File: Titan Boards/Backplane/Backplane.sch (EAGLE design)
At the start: 29 parts, among them P1 39-30-02_S, P3 39-30-04_S

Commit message: Initial schematic design backplane
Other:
- note added: "3.3V/5V Output Connector"
- note added: "Actuator Connector"
- note added: "Battery Balancer Connector"
- note added: "Coprocessor Connector"
- note added: "ESC Connector"
- note added: "Enable Signals Connector"
- note added: "I2C Control Connector"
- note added: "Kill Switch Connector"
- note added: "Lorem ipsum"
- note added: "Schematic Notes:"
- note added: "Switch Connector"
- note added: "Thurster Signal Connector"

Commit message: First final version of Titan Backplane Schematic
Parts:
- removed P1: 39-30-02_S, con-molex-mini-fit:39-30-02_S
- removed P3: 39-30-04_S, con-molex-mini-fit:39-30-04_S
- removed U$5: 929870-01-09_1, 3M_929852_Connector:929870-01-09_1
- removed U$6: 929870-01-09_2, 3M_929852_Connector:929870-01-09_2
- removed U$8: 929870-01-09_4, 3M_929852_Connector:929870-01-09_4
- added 3.3V_CONNECTOR: 39-30-04_S, con-molex-mini-fit:39-30-04_S
- added 5V_CONNECTOR: 39-30-02_S, con-molex-mini-fit:39-30-02_S
- added ACT_CONN_LED, BB_CONN_LED, COPRO_CONN_LED, ESC_CONN_LED: (no value), led:LEDCHIP-LED0603
- added I2C_CONNECTOR: 929870-01-09_4, 3M_929852_Connector:929870-01-09_4
- added KILLSWITCH_CONNECTOR: 929870-01-09_1, 3M_929852_Connector:929870-01-09_1
- added R19, R20, R21, R22: 36, rcl:R-US_R0603
- added THRUSTER_CONNECTOR: 929870-01-09_2, 3M_929852_Connector:929870-01-09_2
- renumbered U$7 to ENABLE_SIGNALS_CONNECTOR
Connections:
- removed net SPARE7: U$1.SPARE7, U$2.SPARE7, U$3.SPARE7, U$4.SPARE7, U$5.SPARE7
- new net ACT_CONN: ACT_CONN_LED.A, U$4.SPARE7
- new net BB_CONN: BB_CONN_LED.A, U$1.SPARE7
- new net COPRO_CONN: COPRO_CONN_LED.A, U$3.SPARE7
- new net ESC_CONN: ESC_CONN_LED.A, U$2.SPARE7
- new net N$12: BB_CONN_LED.C, R19.1
- new net N$13: ESC_CONN_LED.C, R20.1
- new net N$14: COPRO_CONN_LED.C, R21.1
- new net N$15: ACT_CONN_LED.C, R22.1
- net 3.3V: now also 3.3V_CONNECTOR-1.P, I2C_CONNECTOR.3.3V; no longer P3-1.P, U$8.3.3V
- net 5V: now also 5V_CONNECTOR-1.P, I2C_CONNECTOR.5V; no longer P1-1.P, U$8.5V
- net BACKPLANE_SCL: now also I2C_CONNECTOR.BACKPLANE_SCL; no longer U$8.BACKPLANE_SCL
- net BACKPLANE_SDA: now also I2C_CONNECTOR.BACKPLANE_SDA; no longer U$8.BACKPLANE_SDA
- net GND: now also 3.3V_CONNECTOR-3.P, 5V_CONNECTOR-2.P, I2C_CONNECTOR.GND, R19.2, R20.2, R21.2, R22.2; no longer P1-2.P, P3-3.P, U$8.GND
- net KILL_SWITCH: now also KILLSWITCH_CONNECTOR.KILL_SWITCH; no longer U$5.KILL_SWITCH
- net PWM_1: now also THRUSTER_CONNECTOR.PWM_1; no longer U$6.PWM_1
- net PWM_2: now also THRUSTER_CONNECTOR.PWM_2; no longer U$6.PWM_2
- net PWM_3: now also THRUSTER_CONNECTOR.PWM_3; no longer U$6.PWM_3
- net PWM_4: now also THRUSTER_CONNECTOR.PWM_4; no longer U$6.PWM_4
- net PWM_5: now also THRUSTER_CONNECTOR.PWM_5; no longer U$6.PWM_5
- net PWM_6: now also THRUSTER_CONNECTOR.PWM_6; no longer U$6.PWM_6
- net PWM_7: now also THRUSTER_CONNECTOR.PWM_7; no longer U$6.PWM_7
- net PWM_8: now also THRUSTER_CONNECTOR.PWM_8; no longer U$6.PWM_8
- net ROBOT_SCL: now also 3.3V_CONNECTOR-4.P, I2C_CONNECTOR.ROBOT_SCL; no longer P3-4.P, U$8.ROBOT_SCL
- net ROBOT_SDA: now also 3.3V_CONNECTOR-2.P, I2C_CONNECTOR.ROBOT_SDA; no longer P3-2.P, U$8.ROBOT_SDA
- net SPARE2: now also THRUSTER_CONNECTOR.SPARE2; no longer U$6.SPARE2
- net SPARE3: now also I2C_CONNECTOR.SPARE3; no longer U$8.SPARE3
- net SPARE4: now also I2C_CONNECTOR.SPARE4; no longer U$8.SPARE4
- net SPARE5: now also KILLSWITCH_CONNECTOR.SPARE5; no longer U$5.SPARE5
- net SPARE6: now also KILLSWITCH_CONNECTOR.SPARE6; no longer U$5.SPARE6
- net SWITCH_1: now also KILLSWITCH_CONNECTOR.SWITCH_1; no longer U$5.SWITCH_1
- net SWITCH_2: now also KILLSWITCH_CONNECTOR.SWITCH_2; no longer U$5.SWITCH_2
- net SWITCH_3: now also KILLSWITCH_CONNECTOR.SWITCH_3; no longer U$5.SWITCH_3
- net SWITCH_4: now also KILLSWITCH_CONNECTOR.SWITCH_4; no longer U$5.SWITCH_4
- net SWITCH_5: now also KILLSWITCH_CONNECTOR.SWITCH_5; no longer U$5.SWITCH_5
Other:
- note added: "3.3V/5V Connectors"
- note added: "Administrative Notes: Board Name: Titan Backplane Schematic Creation: 08/2020 Schematic Designer: Dylan Trainor Electrical Lead: Phillip Barker"
- note added: "Board Connected Indicators"
- note added: "Part Notes: Board Connectors: 5530843-6 56 Position Female Connector Non Specified - Dual Edge Gold 0.100 in (2.54mm) Black https://www.digikey.com/product-detail/en/te-connectivity-amp-connectors/5530843-6/A31719-ND/770545 Killswitch Connector: 929870-01-09_1 Thruster Signal Connector: 929870-01-09_2 Enable Signals Connector: 929870-01-09_3 I2C Control Connector: 929870-01-09_4 9 Position Recept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"
- note removed: "3.3V/5V Output Connector"
- note removed: "Lorem ipsum"
- moved on the sheet: R1, R10, R11, R12, R13, R14, R15, R16, R17, R18, R2, R3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

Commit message: Titan Backplane Final Version 1
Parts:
- removed 3.3V_CONNECTOR: 39-30-04_S, con-molex-mini-fit:39-30-04_S
- removed ENABLE_SIGNALS_CONNECTOR: 929870-01-09_3, 3M_929852_Connector:929870-01-09_3
- removed I2C_CONNECTOR: 929870-01-09_4, 3M_929852_Connector:929870-01-09_4
- removed KILLSWITCH_CONNECTOR: 929870-01-09_1, 3M_929852_Connector:929870-01-09_1
- removed R1, R10, R11, R12, R13, R14, R2, R3, R4, R5, R6, R7, R8, R9: 10k, rcl:R-US_R0603
- removed THRUSTER_CONNECTOR: 929870-01-09_2, 3M_929852_Connector:929870-01-09_2
- added AUX_I2C_CONNECTOR1, ROBOT_I2C_CONNECTOR: 39-30-04_S, con-molex-mini-fit:39-30-04_S
- added TESTPIN_CONNECTOR: 929870-01-09_4, 3M_929852_Connector:929870-01-09_4
- SWITCH_CONNECTOR: value 39-30-08_S -> 39-30-02_S; device con-molex-mini-fit:39-30-08_S -> con-molex-mini-fit:39-30-02_S
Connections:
- net 12V_ON/OFF: no longer ENABLE_SIGNALS_CONNECTOR.12V_ON/OFF
- net 3.3V: now also AUX_I2C_CONNECTOR1-1.P, ROBOT_I2C_CONNECTOR-1.P, TESTPIN_CONNECTOR.3.3V; no longer 3.3V_CONNECTOR-1.P, I2C_CONNECTOR.3.3V, R10.1, R11.1, R12.1, R13.1, R14.1, R9.1
- net 3.3V_ON/OFF: no longer ENABLE_SIGNALS_CONNECTOR.3.3V_ON/OFF
- net 5V: now also SWITCH_CONNECTOR-1.P, TESTPIN_CONNECTOR.5V; no longer I2C_CONNECTOR.5V, R1.1, R2.1, R3.1, R4.1, R5.1, R6.1, R7.1, R8.1
- net 5V_ON/OFF: no longer ENABLE_SIGNALS_CONNECTOR.5V_ON/OFF
- net ACOUSTIC_ON/OFF: no longer ENABLE_SIGNALS_CONNECTOR.ACOUSTIC_ON/OFF
- net BACKPLANE_SCL: now also TESTPIN_CONNECTOR.BACKPLANE_SCL; no longer I2C_CONNECTOR.BACKPLANE_SCL
- net BACKPLANE_SDA: now also TESTPIN_CONNECTOR.BACKPLANE_SDA; no longer I2C_CONNECTOR.BACKPLANE_SDA
- net CONTROL_SIGNAL: no longer ENABLE_SIGNALS_CONNECTOR.SPARE1
- net GND: now also AUX_I2C_CONNECTOR1-3.P, ROBOT_I2C_CONNECTOR-3.P, SWITCH_CONNECTOR-2.P, TESTPIN_CONNECTOR.GND; no longer 3.3V_CONNECTOR-3.P, ENABLE_SIGNALS_CONNECTOR.GND, I2C_CONNECTOR.GND, SWITCH_CONNECTOR-5.P
- net JETSON_ON/OFF: no longer ENABLE_SIGNALS_CONNECTOR.JETSON_ON/OFF
- net KILL_SWITCH: no longer KILLSWITCH_CONNECTOR.KILL_SWITCH, R9.2, SWITCH_CONNECTOR-2.P
- net MOBO_ON/OFF: no longer ENABLE_SIGNALS_CONNECTOR.MOBO_ON/OFF
- net PLTA_ON/OFF: no longer ENABLE_SIGNALS_CONNECTOR.SPARE8, SWITCH_CONNECTOR-1.P
- net PWM_1: no longer R1.2, THRUSTER_CONNECTOR.PWM_1
- net PWM_2: no longer R2.2, THRUSTER_CONNECTOR.PWM_2
- net PWM_3: no longer R3.2, THRUSTER_CONNECTOR.PWM_3
- net PWM_4: no longer R4.2, THRUSTER_CONNECTOR.PWM_4
- net PWM_5: no longer R5.2, THRUSTER_CONNECTOR.PWM_5
- net PWM_6: no longer R6.2, THRUSTER_CONNECTOR.PWM_6
- net PWM_7: no longer R7.2, THRUSTER_CONNECTOR.PWM_7
- net PWM_8: no longer R8.2, THRUSTER_CONNECTOR.PWM_8
- net ROBOT_SCL: now also AUX_I2C_CONNECTOR1-4.P, ROBOT_I2C_CONNECTOR-4.P, TESTPIN_CONNECTOR.ROBOT_SCL; no longer 3.3V_CONNECTOR-4.P, I2C_CONNECTOR.ROBOT_SCL
- net ROBOT_SDA: now also AUX_I2C_CONNECTOR1-2.P, ROBOT_I2C_CONNECTOR-2.P, TESTPIN_CONNECTOR.ROBOT_SDA; no longer 3.3V_CONNECTOR-2.P, I2C_CONNECTOR.ROBOT_SDA
- net SPARE2: no longer THRUSTER_CONNECTOR.SPARE2
- net SPARE3: now also TESTPIN_CONNECTOR.SPARE3; no longer I2C_CONNECTOR.SPARE3
- net SPARE4: now also TESTPIN_CONNECTOR.SPARE4; no longer I2C_CONNECTOR.SPARE4
- net SPARE5: no longer KILLSWITCH_CONNECTOR.SPARE5
- net SPARE6: no longer KILLSWITCH_CONNECTOR.SPARE6
- net SWITCH_1: no longer KILLSWITCH_CONNECTOR.SWITCH_1, R10.2, SWITCH_CONNECTOR-3.P
- net SWITCH_2: no longer KILLSWITCH_CONNECTOR.SWITCH_2, R11.2, SWITCH_CONNECTOR-4.P
- net SWITCH_3: no longer KILLSWITCH_CONNECTOR.SWITCH_3, R12.2, SWITCH_CONNECTOR-6.P
- net SWITCH_4: no longer KILLSWITCH_CONNECTOR.SWITCH_4, R13.2, SWITCH_CONNECTOR-7.P
- net SWITCH_5: no longer KILLSWITCH_CONNECTOR.SWITCH_5, R14.2, SWITCH_CONNECTOR-8.P
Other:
- note added: "5V Connector"
- note added: "Auxillary I2C Connector"
- note added: "Part Notes: Board Connectors: 5530843-6 56 Position Female Connector Non Specified - Dual Edge Gold 0.100 in (2.54mm) Black https://www.digikey.com/product-detail/en/te-connectivity-amp-connectors/5530843-6/A31719-ND/770545 Test Pin Connector: 929870-01-09 9 Position Receptacle Connector Through Hole https://www.digikey.com/product-detail/en/3m/929870-01-09-RA/929870-01-09-RA-ND/1239312 Board Con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"
- note added: "Robot I2C Connector"
- note added: "Test Pin Connector"
- note removed: "3.3V/5V Connectors"
- note removed: "Enable Signals Connector"
- note removed: "I2C Control Connector"
- note removed: "Kill Switch Connector"
- note removed: "Part Notes: Board Connectors: 5530843-6 56 Position Female Connector Non Specified - Dual Edge Gold 0.100 in (2.54mm) Black https://www.digikey.com/product-detail/en/te-connectivity-amp-connectors/5530843-6/A31719-ND/770545 Killswitch Connector: 929870-01-09_1 Thruster Signal Connector: 929870-01-09_2 Enable Signals Connector: 929870-01-09_3 I2C Control Connector: 929870-01-09_4 9 Position Recept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"
- note removed: "Thurster Signal Connector"

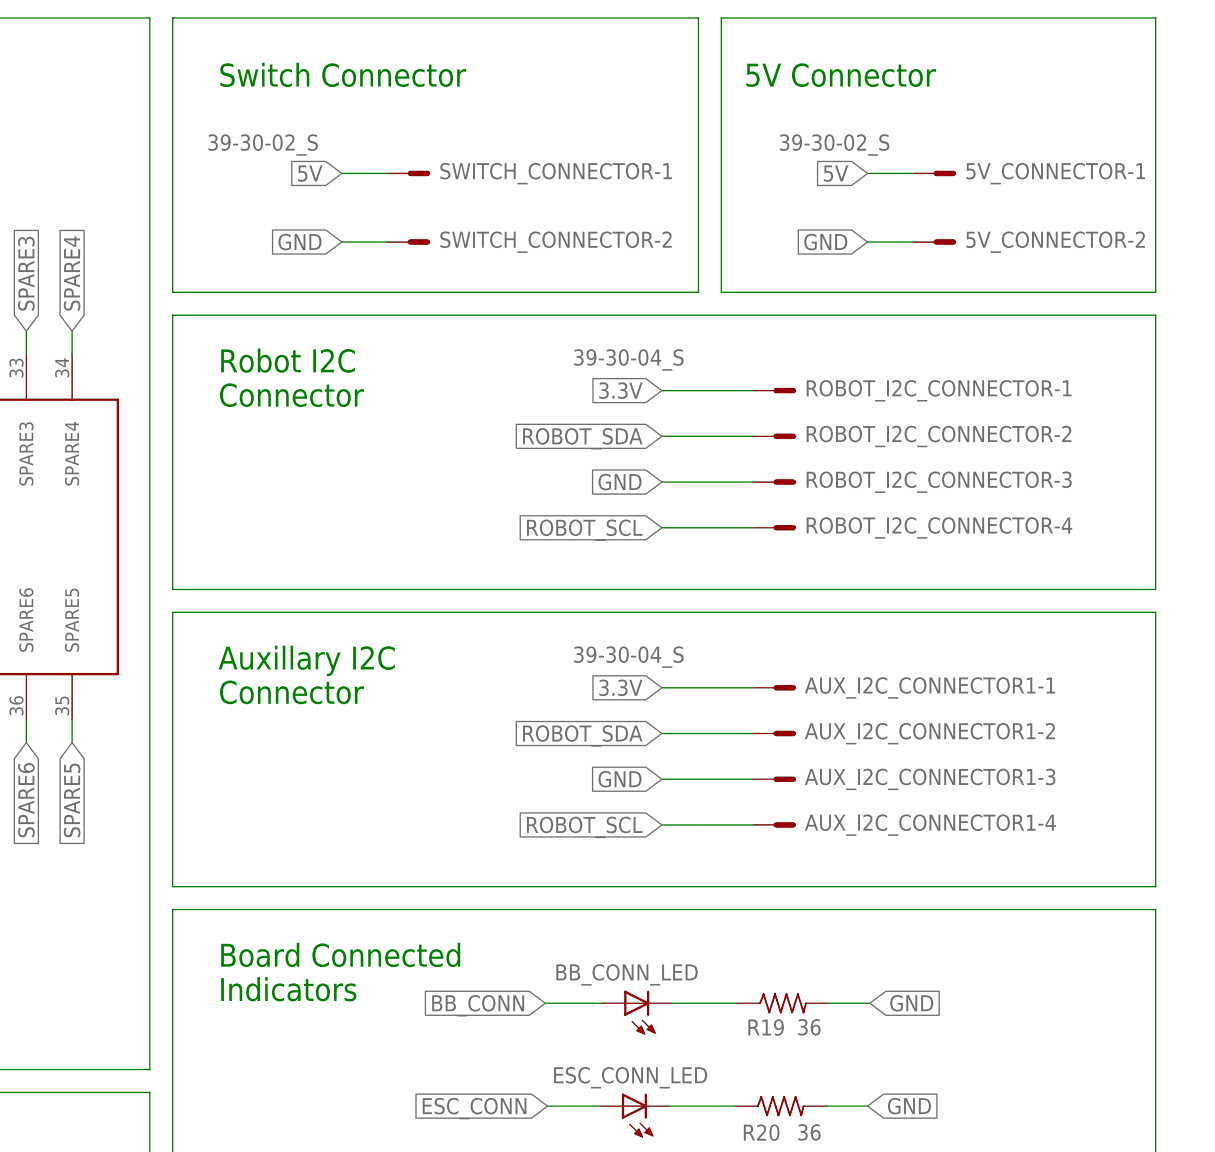
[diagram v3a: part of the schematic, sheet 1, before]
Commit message: Backplane connector and spacing revisions
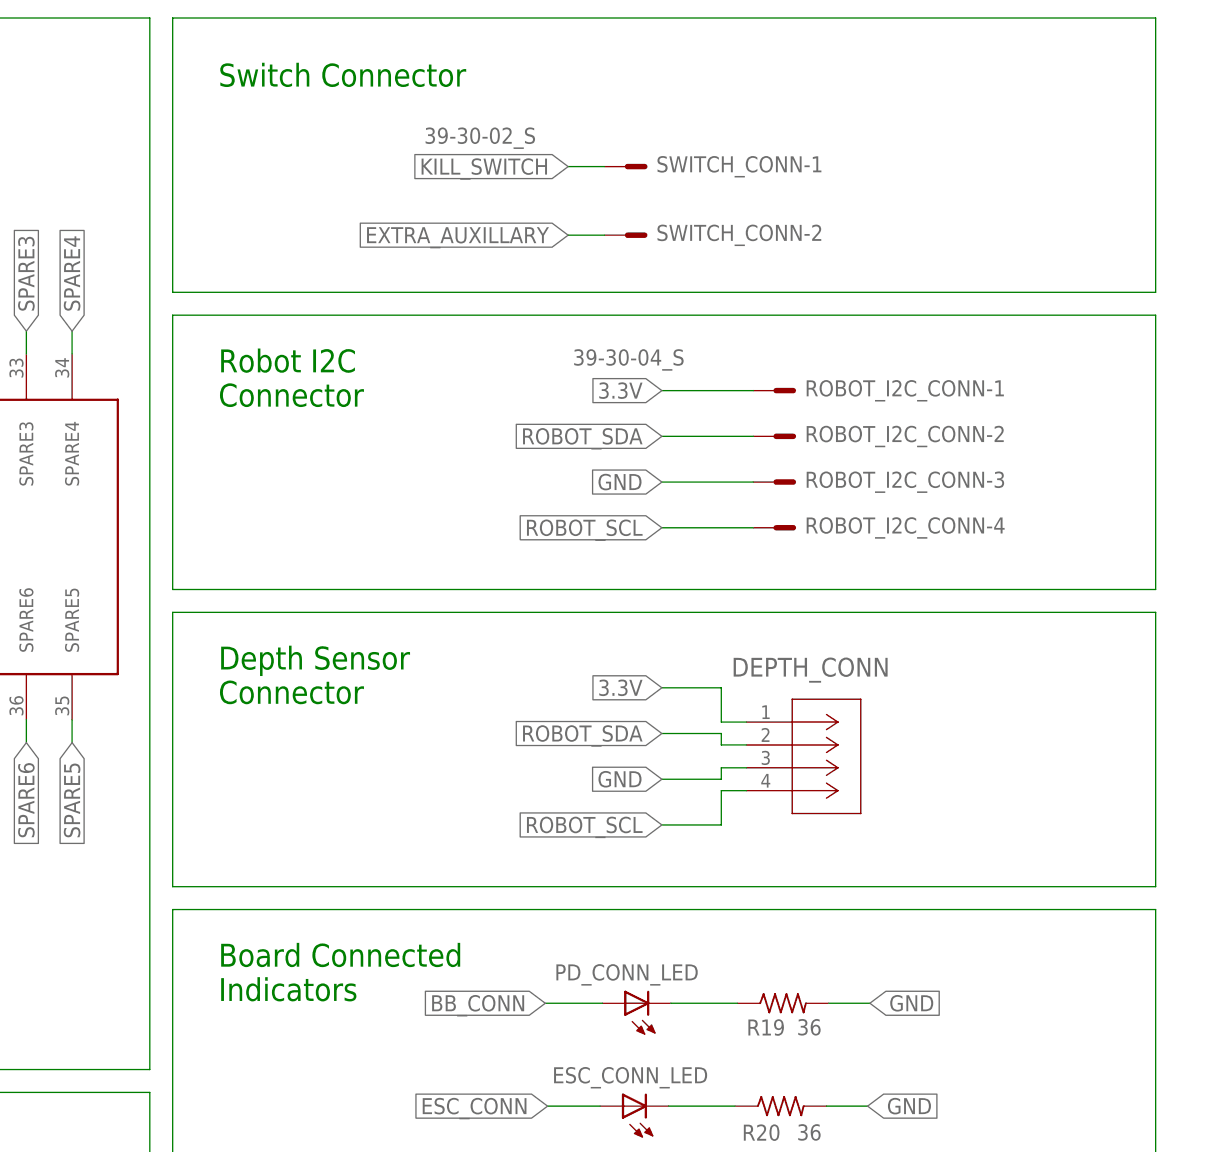
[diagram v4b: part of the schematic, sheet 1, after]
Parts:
- removed 5V_CONNECTOR, SWITCH_CONNECTOR: 39-30-02_S, con-molex-mini-fit:39-30-02_S
- removed AUX_I2C_CONNECTOR1: 39-30-04_S, con-molex-mini-fit:39-30-04_S
- added DEPTH_CONN: DF13-4P-1.25DSA, DF13-4P-125DSA_Connector:DF13-4P-1.25DSA
- added SWITCH_CONN: 39-30-02_S, con-molex-mini-fit:39-30-02_S
- renumbered BB_CONN_LED to PD_CONN_LED, ROBOT_I2C_CONNECTOR to ROBOT_I2C_CONN
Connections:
- new net EXTRA_AUXILLARY: SWITCH_CONN-2.P
- net 3.3V: now also DEPTH_CONN.1; no longer AUX_I2C_CONNECTOR1-1.P
- net 5V: no longer 5V_CONNECTOR-1.P, SWITCH_CONNECTOR-1.P
- net GND: now also DEPTH_CONN.3; no longer 5V_CONNECTOR-2.P, AUX_I2C_CONNECTOR1-3.P, SWITCH_CONNECTOR-2.P
- net KILL_SWITCH: now also SWITCH_CONN-1.P
- net ROBOT_SCL: now also DEPTH_CONN.4; no longer AUX_I2C_CONNECTOR1-4.P
- net ROBOT_SDA: now also DEPTH_CONN.2; no longer AUX_I2C_CONNECTOR1-2.P
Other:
- note added: "Depth Sensor Connector"
- note removed: "5V Connector"
- note removed: "Auxillary I2C Connector"

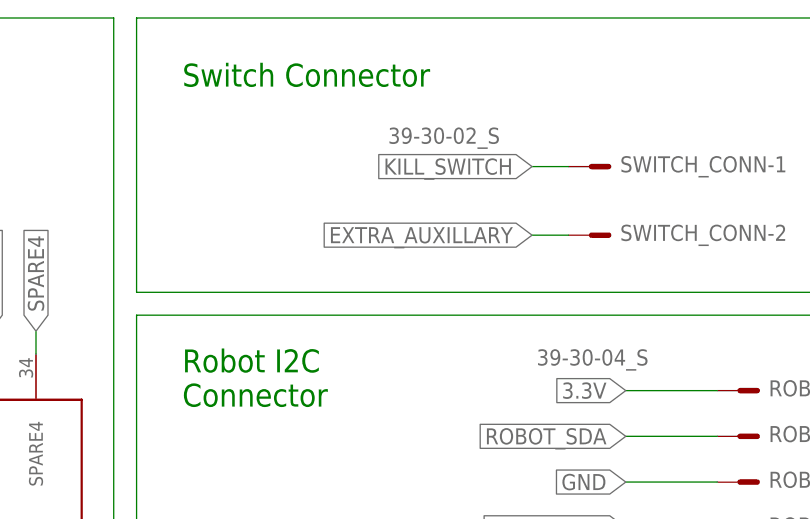
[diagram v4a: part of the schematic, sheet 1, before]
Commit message: backplane reorientation changes
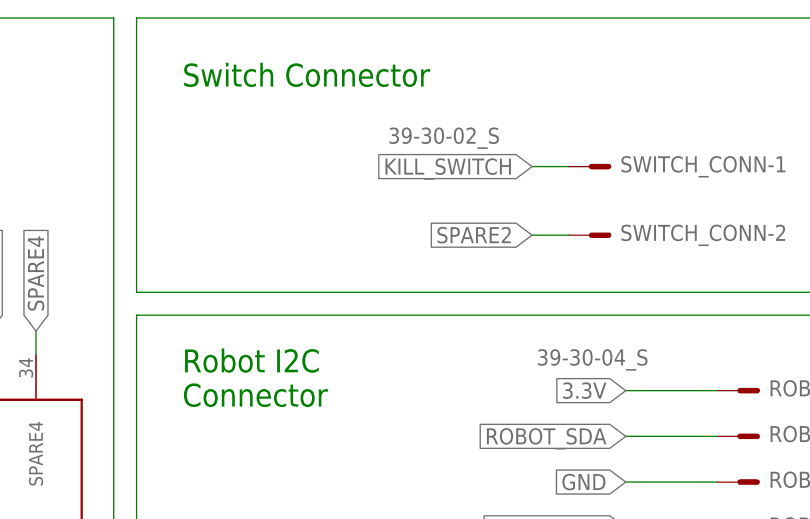
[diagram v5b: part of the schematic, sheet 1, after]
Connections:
- removed net EXTRA_AUXILLARY: SWITCH_CONN-2.P
- net SPARE2: now also SWITCH_CONN-2.P
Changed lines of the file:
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@@
 <pinref part="U$4" gate="G$1" pin="SPARE2"/>
+</segment>
+<segment>
+<label x="308.102" y="227.33" size="1.778" layer="95" rot="R180" xref="yes"/>
+<wire x1="312.166" y1="227.33" x2="308.102" y2="227.33" width="0.1524" layer="91"/>
+<pinref part="SWITCH_CONN" gate="-2" pin="P"/>
 </segment>
 </net>
@@
 </segment>
 </net>
-<net name="EXTRA_AUXILLARY" class="0">
-<segment>
-<label x="308.102" y="227.33" size="1.778" layer="95" rot="R180" xref="yes"/>
-<wire x1="312.166" y1="227.33" x2="308.102" y2="227.33" width="0.1524" layer="91"/>
-<pinref part="SWITCH_CONN" gate="-2" pin="P"/>
-</segment>
-</net>
